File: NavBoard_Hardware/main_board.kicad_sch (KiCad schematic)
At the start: 13 parts, among them J1 8P8C_LED_Shielded, J10 Conn_01x16, J11 Conn_01x16, J12 Conn_01x24, J8 Conn_01x06, J9 Conn_01x24

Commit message: Created adapter symbols and footprints
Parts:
- removed J10, J11: Conn_01x16, symbol Connector_Generic:Conn_01x16
- removed J12, J9: Conn_01x24, symbol Connector_Generic:Conn_01x24
- added J? (x2): 24Pin_To_16Pin_2.54mm_Alt, Nav_Board:24Pin_To_16Pin_2.54mm, symbol Nav_Board:24Pin_To_16Pin_2.54mm_Alt
- gave numbers to parts that had none: 5
- renumbered C1 to C15, J1 to J2, J8 to J3
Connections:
- net Pin10L: now also J?.10
- net Pin10L_Small: now also J?.18
- net Pin10R: now also J?.39
- net Pin10R_Small: now also J?.31
- net Pin11L: now also J?.11
- net Pin11L_Small: now also J?.19
- net Pin11R: now also J?.38
- net Pin11R_Small: now also J?.30
- net Pin12L: now also J?.12
- net Pin12L_Small: now also J?.20
- net Pin12R: now also J?.37
- net Pin12R_Small: now also J?.29
- net Pin13L: now also J?.13
- net Pin13L_Small: now also J?.21
- net Pin13R: now also J?.36
- net Pin13R_Small: now also J?.28
- net Pin14L: now also J?.14
- net Pin14L_Small: now also J?.22
- net Pin14R: now also J?.35
- net Pin14R_Small: now also J?.27
- net Pin15L: now also J?.15
- net Pin15L_Small: now also J?.23
- net Pin15R: now also J?.34
- net Pin15R_Small: now also J?.26
- net Pin16L: now also J?.16
- net Pin16L_Small: now also J?.24
- net Pin16R: now also J?.33
- net Pin16R_Small: now also J?.25
- net Pin17L: now also J?.17
- net Pin17R: now also J?.32
- net Pin18L: now also J?.18
- net Pin18R: now also J?.31
- net Pin19L: now also J?.19
- net Pin19R: now also J?.30
- net Pin1L: now also J?.1
- net Pin1L_Small: now also J?.9
- net Pin1R: now also J?.48
- net Pin1R_Small: now also J?.40
- net Pin20L: now also J?.20
- net Pin20R: now also J?.29
- net Pin21L: now also J?.21
- net Pin21R: now also J?.28
- net Pin22L: now also J?.22
- net Pin22R: now also J?.27
- net Pin23L: now also J?.23
- net Pin23R: now also J?.26
- net Pin24L: now also J?.24
- net Pin24R: now also J?.25
- net Pin2L: now also J?.2
- net Pin2L_Small: now also J?.10
- net Pin2R: now also J?.47
- net Pin2R_Small: now also J?.39
- net Pin3L: now also J?.3
- net Pin3L_Small: now also J?.11
- net Pin3R: now also J?.46
- net Pin3R_Small: now also J?.38
- net Pin4L: now also J?.4
- net Pin4L_Small: now also J?.12
- net Pin4R: now also J?.45
- net Pin4R_Small: now also J?.37
- net Pin5L: now also J?.5
- net Pin5L_Small: now also J?.13
- net Pin5R: now also J?.44
- net Pin5R_Small: now also J?.36
- net Pin6L: now also J?.6
- net Pin6L_Small: now also J?.14
- net Pin6R: now also J?.43
- net Pin6R_Small: now also J?.35
- net Pin7L: now also J?.7
- net Pin7L_Small: now also J?.15
- net Pin7R: now also J?.42
- net Pin7R_Small: now also J?.34
- net Pin8L: now also J?.8
- net Pin8L_Small: now also J?.16
- net Pin8R: now also J?.41
- net Pin8R_Small: now also J?.33
- net Pin9L: now also J?.9
- net Pin9L_Small: now also J?.17
- net Pin9R: now also J?.40
- net Pin9R_Small: now also J?.32

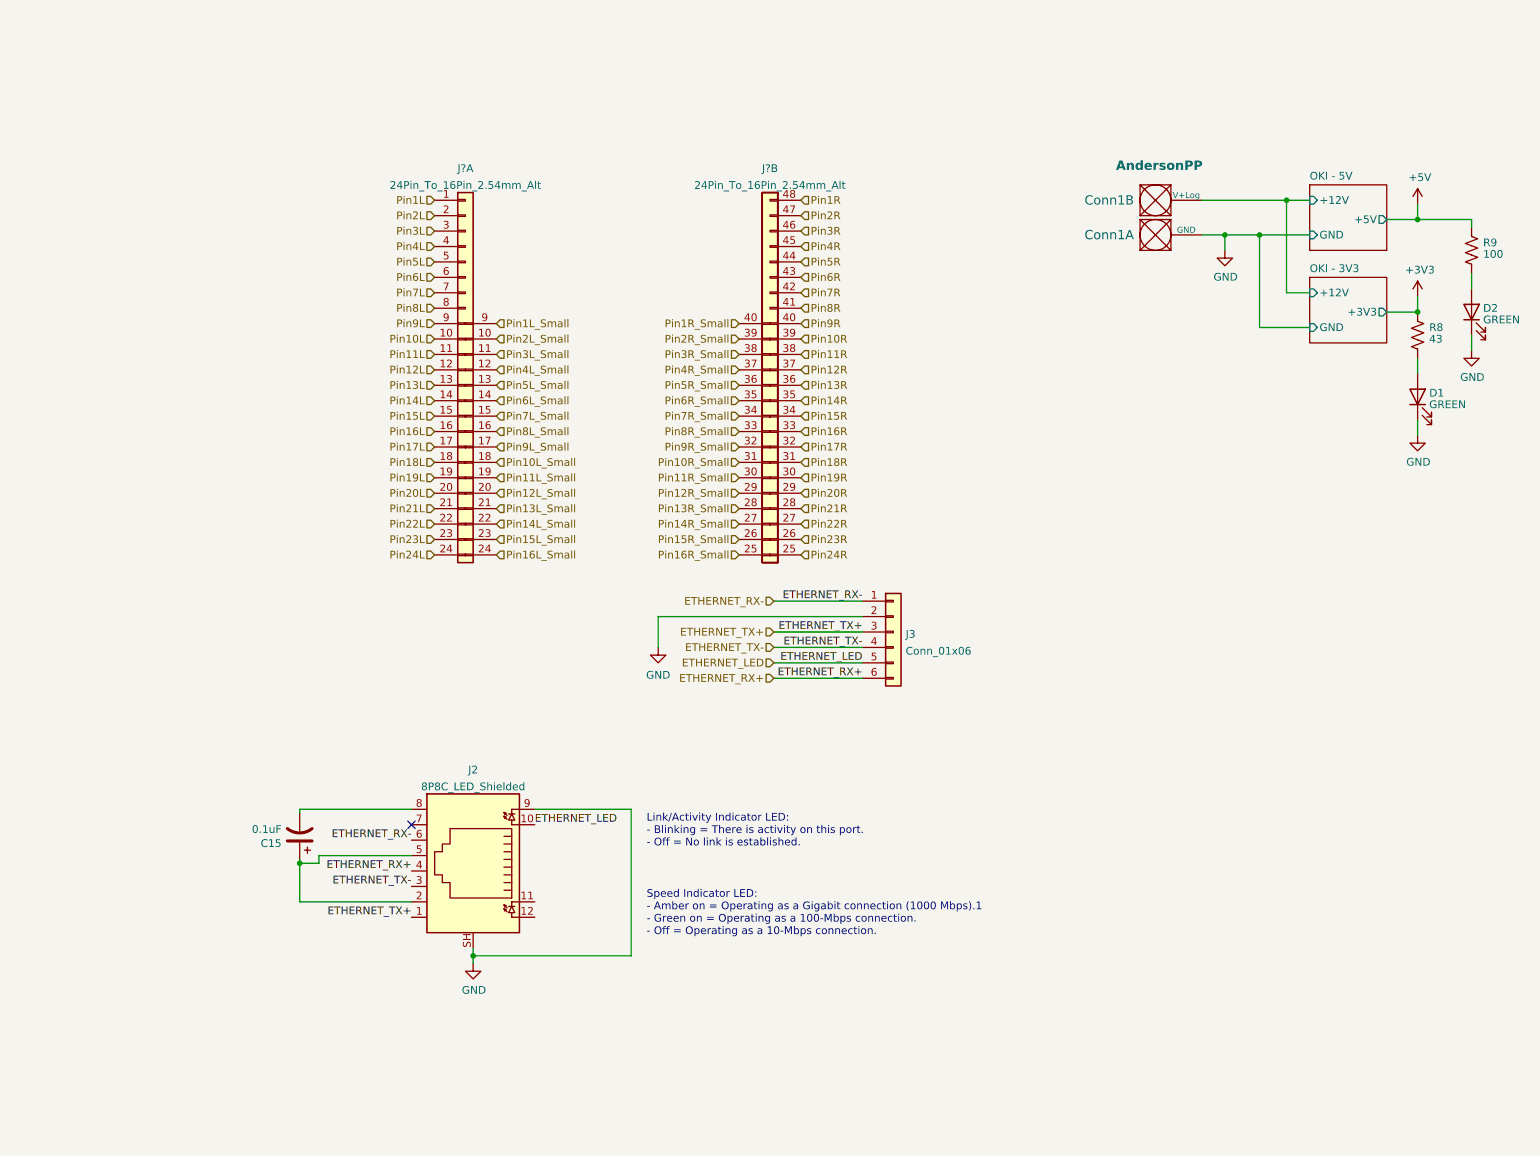
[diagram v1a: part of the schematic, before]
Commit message: Added connectors, cleaned up file directory
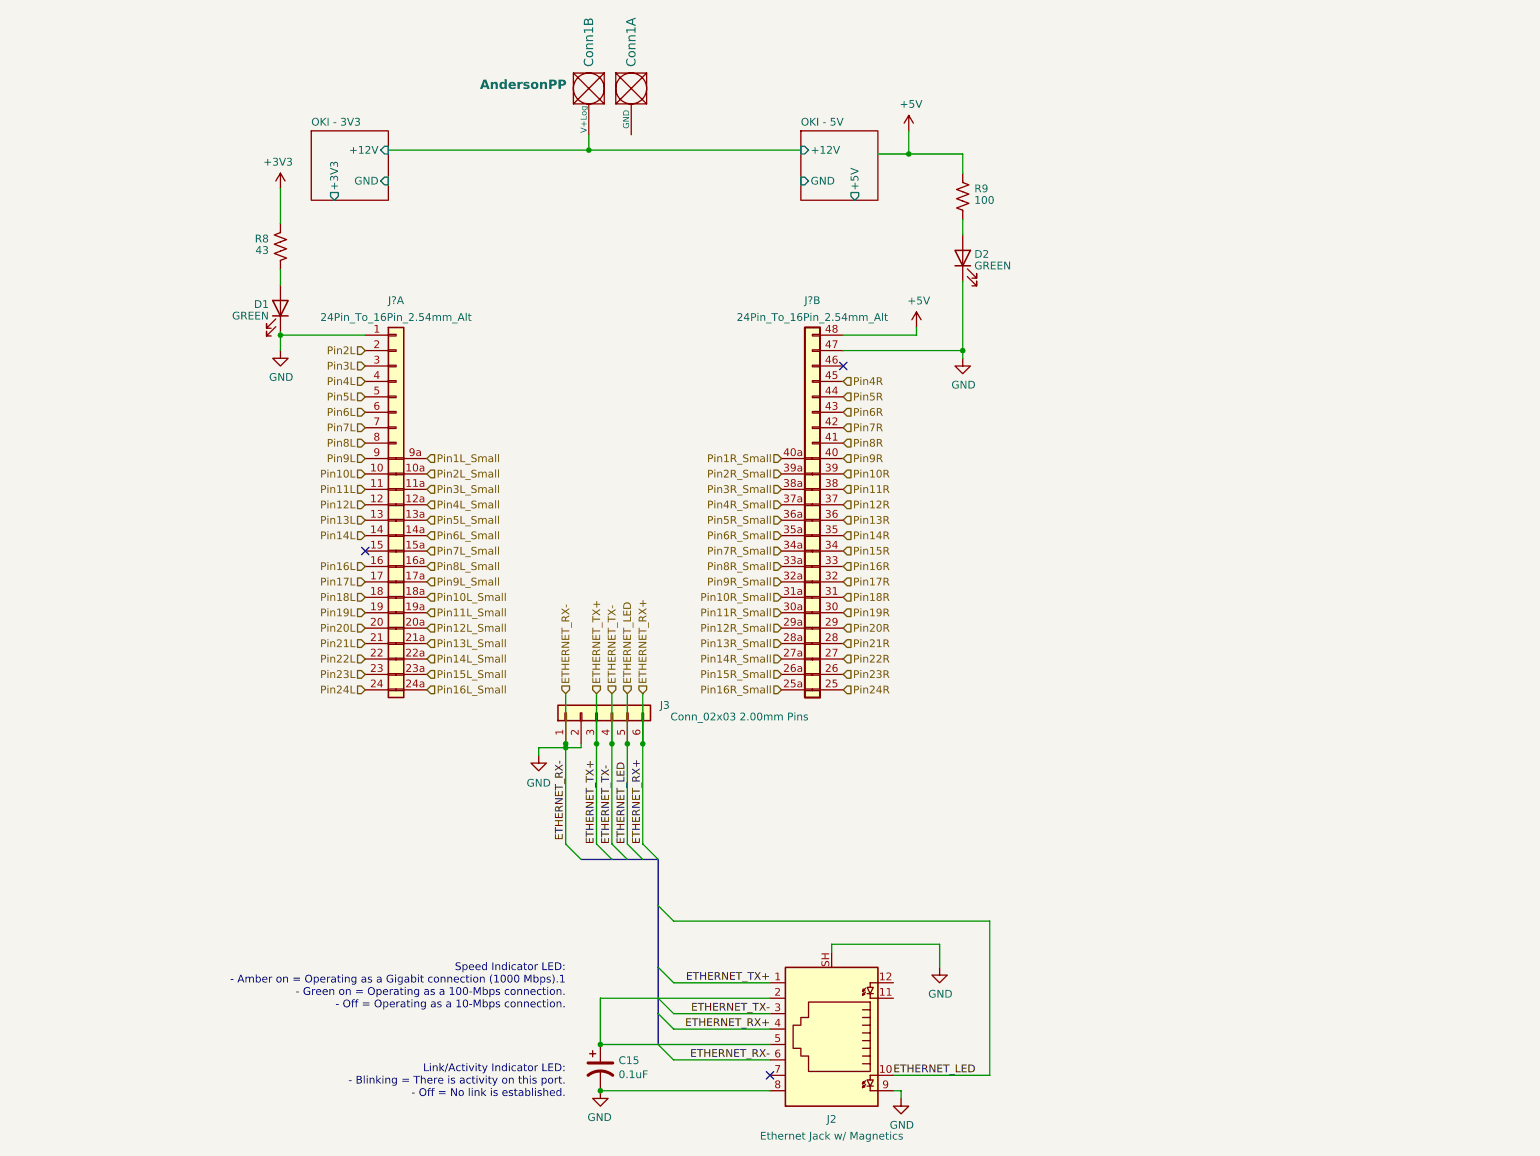
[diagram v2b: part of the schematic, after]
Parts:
- J2: value 8P8C_LED_Shielded -> Ethernet Jack w/ Magnetics; footprint Connector_RJ:RJ45_Amphenol_RJHSE538X -> Connector_RJ:RJ45_Cetus_J1B1211CCD_Horizontal; Part Opt 1 (none) -> Link-PP LPJ4012AHNL; Part Opt 2 (none) -> Cetus J1B1211CCD
- J3: value Conn_01x06 -> Conn_02x03 2.00mm Pins; footprint (none) -> Connector_PinSocket_2.00mm:PinSocket_2x03_P2.00mm_Vertical
- J? (x2): footprint Nav_Board:24Pin_To_16Pin_2.54mm -> Nav_Board:24Pin_To_16Pin_2.54mm_Separate_Pins; symbol Nav_Board:24Pin_To_16Pin_2.54mm_Alt -> Nav_Board:24Pin_To_16Pin_2.54mm_Separate_Pins_Alt
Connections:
- net ETHERNET_RX- is gone; now on net GND: J2.6, J3.1 (Pin_1)
- net Pin1L is gone; now on net GND: J?.1
- net Pin1R is gone; now on net +5V: J?.48
- net Pin2R is gone; now on net GND: J?.47
- net GND: now also C15.2, J2.8; no longer Conn1.1 (GND)
- net Pin10L_Small: now also J?.18a; no longer J?.18
- net Pin10R_Small: now also J?.31a; no longer J?.31
- net Pin11L_Small: now also J?.19a; no longer J?.19
- net Pin11R_Small: now also J?.30a; no longer J?.30
- net Pin12L_Small: now also J?.20a; no longer J?.20
- net Pin12R_Small: now also J?.29a; no longer J?.29
- net Pin13L_Small: now also J?.21a; no longer J?.21
- net Pin13R_Small: now also J?.28a; no longer J?.28
- net Pin14L_Small: now also J?.22a; no longer J?.22
- net Pin14R_Small: now also J?.27a; no longer J?.27
- net Pin15L_Small: now also J?.23a; no longer J?.23
- net Pin15R_Small: now also J?.26a; no longer J?.26
- net Pin16L_Small: now also J?.24a; no longer J?.24
- net Pin16R_Small: now also J?.25a; no longer J?.25
- net Pin1L_Small: now also J?.9a; no longer J?.9
- net Pin1R_Small: now also J?.40a; no longer J?.40
- net Pin2L_Small: now also J?.10a; no longer J?.10
- net Pin2R_Small: now also J?.39a; no longer J?.39
- net Pin3L_Small: now also J?.11a; no longer J?.11
- net Pin3R_Small: now also J?.38a; no longer J?.38
- net Pin4L_Small: now also J?.12a; no longer J?.12
- net Pin4R_Small: now also J?.37a; no longer J?.37
- net Pin5L_Small: now also J?.13a; no longer J?.13
- net Pin5R_Small: now also J?.36a; no longer J?.36
- net Pin6L_Small: now also J?.14a; no longer J?.14
- net Pin6R_Small: now also J?.35a; no longer J?.35
- net Pin7L_Small: now also J?.15a; no longer J?.15
- net Pin7R_Small: now also J?.34a; no longer J?.34
- net Pin8L_Small: now also J?.16a; no longer J?.16
- net Pin8R_Small: now also J?.33a; no longer J?.33
- net Pin9L_Small: now also J?.17a; no longer J?.17
- net Pin9R_Small: now also J?.32a; no longer J?.32
- net Pin15L: no longer names the net of J?.15
- net Pin3R: no longer names the net of J?.46
- no-connect marks 1 -> 3
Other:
- moved on the sheet: C15, Conn1A, Conn1B, D1, D2, J2, J3, J?A, J?B, R8, R9

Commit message: Updated BMI component sheet from Navboard_2023_rev2
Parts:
- J3: value Conn_02x03 2.00mm Pins -> Conn_02x03; Field4 (none) -> 2.00mm Pins
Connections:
- net GND: now also Conn1.1 (GND)
- net OKI - 3V3/+12V renamed +12V
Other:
- moved on the sheet: Conn1A, Conn1B, D1, D2, J?A, J?B, R8, R9

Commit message: Most schematic connections completed
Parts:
- J?: value 24Pin_To_16Pin_2.54mm_Alt -> 24Pin To 16Pin; 16Pin Type (none) -> 2.54mm Pins; 24Pin Type (none) -> 2.54mm Sockets
- J?: value 24Pin_To_16Pin_2.54mm_Alt -> 24Pin to 16Pin; 16Pin Type (none) -> 2.54mm Pins; 24Pin Type (none) -> 2.54mm Sockets
- R8: value 43 -> 43Ω
- R9: value 100 -> 100Ω
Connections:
- net GND: no longer J2.6, J3.1 (Pin_1)
- new net ETHERNET_RX-: J2.6, J3.1 (Pin_1)

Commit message: Annotated Schematic, assigned footprints, recovered accelerometer footprints
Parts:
- J3: Field4 2.00mm Pins -> 2.00mm Sockets
- gave numbers to parts that had none: 2
- renumbered J2 to J4
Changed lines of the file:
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@@
   (symbol (lib_id "power:+5V") (at 144.78 62.23 0) (unit 1)
     (in_bom yes) (on_board yes)
-    (property "Reference" "#PWR?" (id 0) (at 144.78 66.04 0)
+    (property "Reference" "#PWR026" (id 0) (at 144.78 66.04 0)
       (effects (font (size 1.27 1.27)) hide)
     )
@@
   (symbol (lib_id "power:GND") (at 142.24 185.42 0) (unit 1)
     (in_bom yes) (on_board yes)
-    (property "Reference" "#PWR024" (id 0) (at 142.24 191.77 0)
+    (property "Reference" "#PWR032" (id 0) (at 142.24 191.77 0)
       (effects (font (size 1.27 1.27)) hide)
     )
@@
   (symbol (lib_id "power:+12V") (at 93.345 34.925 0) (unit 1)
     (in_bom yes) (on_board yes) (fields_autoplaced)
-    (property "Reference" "#PWR?" (id 0) (at 93.345 38.735 0)
+    (property "Reference" "#PWR022" (id 0) (at 93.345 38.735 0)
       (effects (font (size 1.27 1.27)) hide)
     )
@@
   (symbol (lib_id "power:GND") (at 92.71 184.15 0) (mirror y) (unit 1)
     (in_bom yes) (on_board yes)
-    (property "Reference" "#PWR?" (id 0) (at 92.71 190.5 0)
+    (property "Reference" "#PWR031" (id 0) (at 92.71 190.5 0)
       (effects (font (size 1.27 1.27)) hide)
     )
@@
   (symbol (lib_id "power:GND") (at 93.345 45.085 0) (unit 1)
     (in_bom yes) (on_board yes)
-    (property "Reference" "#PWR?" (id 0) (at 93.345 51.435 0)
+    (property "Reference" "#PWR025" (id 0) (at 93.345 51.435 0)
       (effects (font (size 1.27 1.27)) hide)
     )
@@
   (symbol (lib_id "power:+5V") (at 152.4 43.815 0) (unit 1)
     (in_bom yes) (on_board yes)
-    (property "Reference" "#PWR027" (id 0) (at 152.4 47.625 0)
+    (property "Reference" "#PWR024" (id 0) (at 152.4 47.625 0)
       (effects (font (size 1.27 1.27)) hide)
     )
@@
   (symbol (lib_id "Connector:8P8C_LED_Shielded") (at 130.81 173.99 180) (unit 1)
     (in_bom yes) (on_board yes) (fields_autoplaced)
-    (property "Reference" "J2" (id 0) (at 130.81 188.8395 0))
+    (property "Reference" "J4" (id 0) (at 130.81 188.8395 0))
     (property "Value" "Ethernet Jack w/ Magnetics" (id 1) (at 130.81 191.6146 0))
     (property "Footprint" "Connector_RJ:RJ45_Cetus_J1B1211CCD_Horizontal" (id 2) (at 130.81 174.625 90)
@@
   (symbol (lib_id "power:+3V3") (at 40.005 43.815 0) (mirror y) (unit 1)
     (in_bom yes) (on_board yes)
-    (property "Reference" "#PWR028" (id 0) (at 40.005 47.625 0)
+    (property "Reference" "#PWR023" (id 0) (at 40.005 47.625 0)
       (effects (font (size 1.27 1.27)) hide)
     )
@@
   (symbol (lib_id "power:GND") (at 152.4 67.31 0) (unit 1)
     (in_bom yes) (on_board yes)
-    (property "Reference" "#PWR?" (id 0) (at 152.4 73.66 0)
+    (property "Reference" "#PWR028" (id 0) (at 152.4 73.66 0)
       (effects (font (size 1.27 1.27)) hide)
     )
@@
   (symbol (lib_id "Nav_Board:24Pin_To_16Pin_2.54mm_Separate_Pins_Alt") (at 59.055 62.23 0) (unit 1)
     (in_bom yes) (on_board yes)
-    (property "Reference" "J?" (id 0) (at 59.055 57.15 0))
+    (property "Reference" "J1" (id 0) (at 59.055 57.15 0))
     (property "Value" "24Pin To 16Pin" (id 1) (at 59.055 59.9251 0))
     (property "Footprint" "Nav_Board:24Pin_To_16Pin_2.54mm_Separate_Pins" (id 2) (at 59.055 59.055 0)
@@
       (effects (font (size 1.27 1.27)) hide)
     )
-    (property "Field4" " 2.00mm Pins" (id 4) (at 92.71 102.235 90))
+    (property "Field4" " 2.00mm Sockets" (id 4) (at 92.71 102.235 90))
     (pin "1")
     (pin "2")
@@
   (symbol (lib_id "power:GND") (at 148.59 163.83 0) (unit 1)
     (in_bom yes) (on_board yes)
-    (property "Reference" "#PWR?" (id 0) (at 148.59 170.18 0)
+    (property "Reference" "#PWR030" (id 0) (at 148.59 170.18 0)
       (effects (font (size 1.27 1.27)) hide)
     )
@@
   (symbol (lib_id "power:GND") (at 40.005 66.04 0) (unit 1)
     (in_bom yes) (on_board yes)
-    (property "Reference" "#PWR?" (id 0) (at 40.005 72.39 0)
+    (property "Reference" "#PWR027" (id 0) (at 40.005 72.39 0)
       (effects (font (size 1.27 1.27)) hide)
     )
@@
   (symbol (lib_id "power:GND") (at 82.55 128.905 0) (unit 1)
     (in_bom yes) (on_board yes) (fields_autoplaced)
-    (property "Reference" "#PWR025" (id 0) (at 82.55 135.255 0)
+    (property "Reference" "#PWR029" (id 0) (at 82.55 135.255 0)
       (effects (font (size 1.27 1.27)) hide)
     )
@@
   (symbol (lib_id "Nav_Board:24Pin_To_16Pin_2.54mm_Separate_Pins_Alt") (at 127.635 62.23 0) (mirror y) (unit 2)
     (in_bom yes) (on_board yes)
-    (property "Reference" "J?" (id 0) (at 127.635 57.15 0))
+    (property "Reference" "J2" (id 0) (at 127.635 57.15 0))
     (property "Value" "24Pin to 16Pin" (id 1) (at 127.635 59.9251 0))
     (property "Footprint" "Nav_Board:24Pin_To_16Pin_2.54mm_Separate_Pins" (id 2) (at 127.635 59.055 0)
